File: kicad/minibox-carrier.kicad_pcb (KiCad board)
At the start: 2 copper layers, 120 x 112 mm, 14 parts, among them J1 ESP32-S3 LEFT - USB AT TOP, J11 THREE-KEY CABLE KeyA KeyB Key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, J12 JOYSTICK CABLE G V X Y K, J2 ESP32-S3 RIGHT - USB AT TOP, J3 INMP441 2x3 VDD GND / SCK WS 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, J4 MAX98357A LRC BCLK DIN GAIN S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, J5 PCF8563T CLK INT SDA SCL VCC 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, J6 ST7796 14-PIN DISPLAY HEADER, J7 5.08mm wire terminal, J8 5.08mm wire terminal

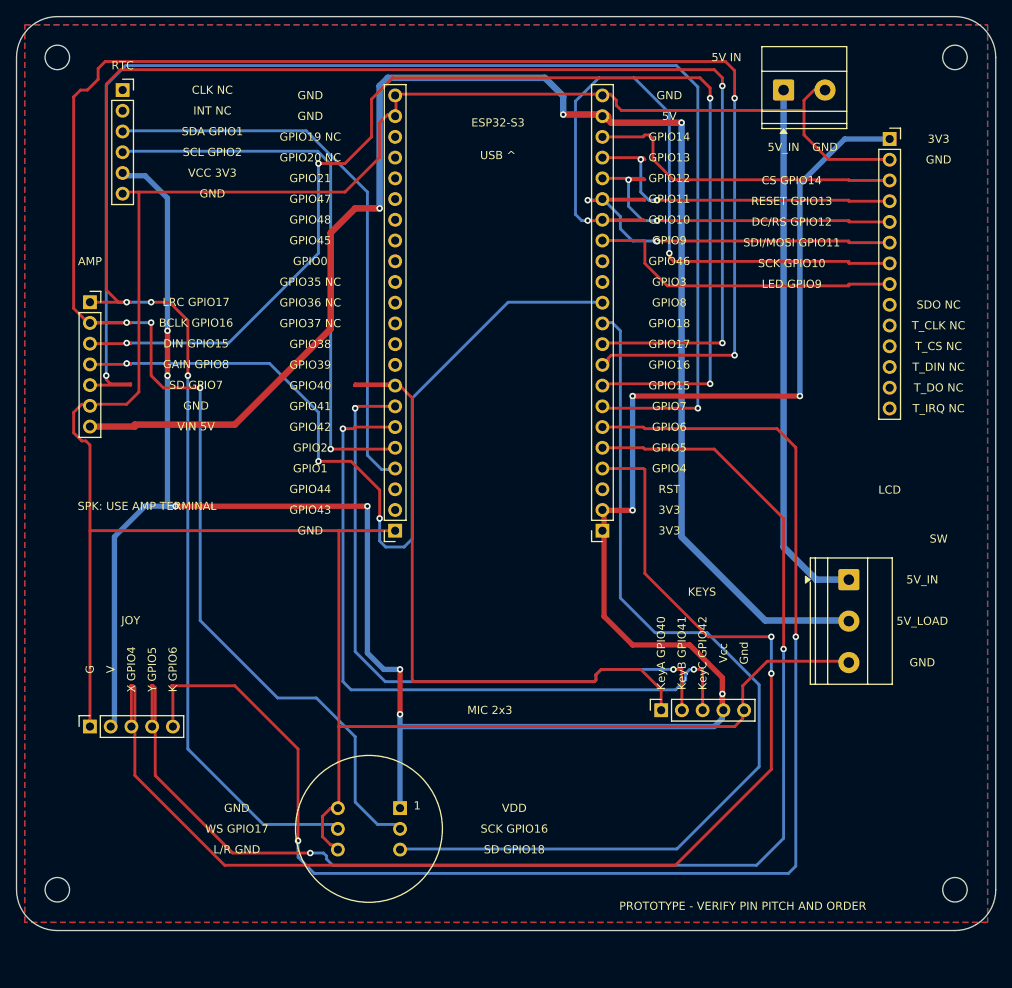
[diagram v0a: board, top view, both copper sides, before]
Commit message: Allocate GPIOs by carrier layout and move cable interfaces upward
Keep joystick axes on ADC1 GPIO1/2, keypad on GPIO4/5/6, local I2S on GPIO39/40/41 and RTC on GPIO47/21. Synchronize firmware, labels, two-layer Gerbers and PNG legends.

Co-authored-by: Copilot App <223556219+Copilot@users.noreply.github.com>
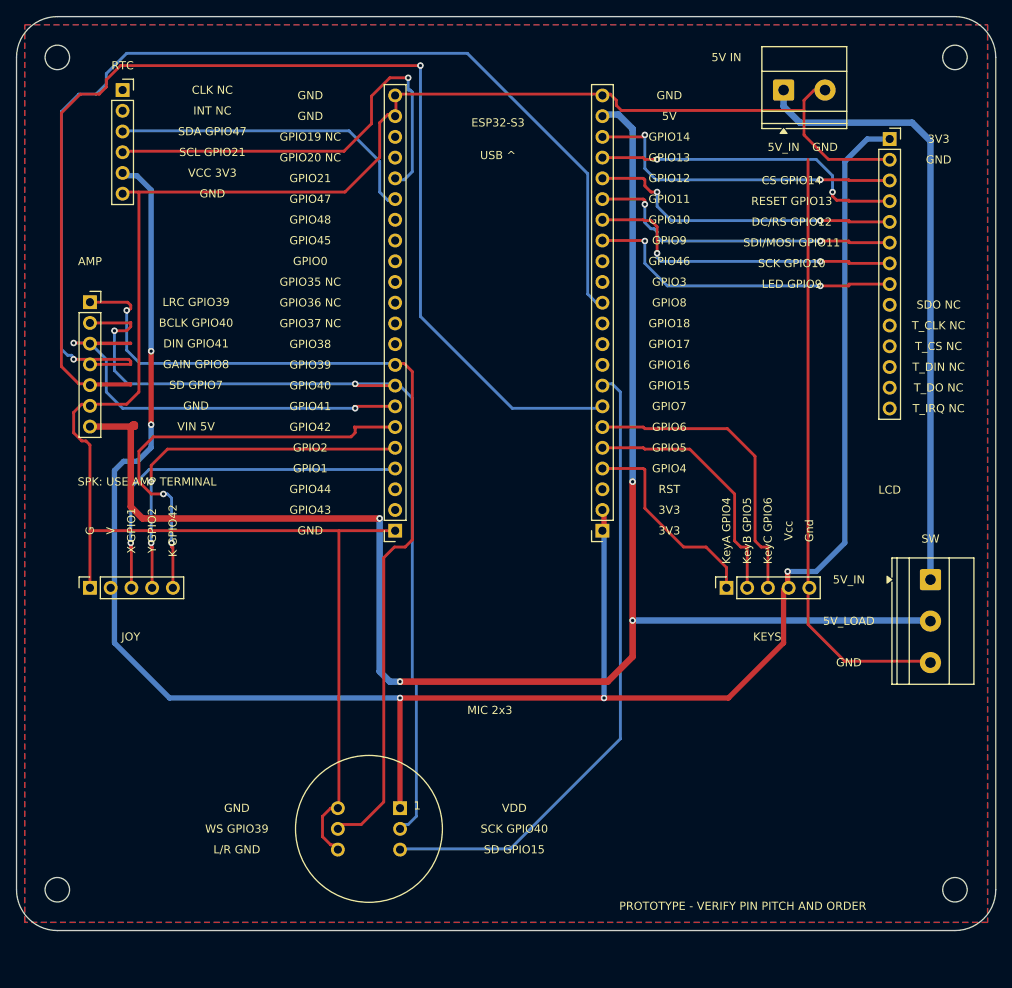
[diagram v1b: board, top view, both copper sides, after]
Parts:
- moved J11 17.0 mm to (90.0, 73.0)
- moved J12 17.0 mm to (12.0, 73.0)
- moved J7 10.0 mm to (115.0, 72.0)
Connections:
- J1 pad 10: I2S_WS -> GPIO17
- J1 pad 11: MIC_SD -> GPIO18
- J1 pad 4: GPIO4 -> BUTTON1
- J1 pad 5: GPIO5 -> RECORD
- J1 pad 6: GPIO6 -> BUTTON3
- J1 pad 8: AUDIO_DIN -> MIC_SD
- J1 pad 9: I2S_BCLK -> GPIO16
- J12 pad 3: GPIO4 -> GPIO1
- J12 pad 4: GPIO5 -> GPIO2
- J12 pad 5: GPIO6 -> GPIO42
- J2 pad 17: GPIO47 -> RTC_SDA
- J2 pad 18: GPIO21 -> RTC_SCL
- J2 pad 4: RTC_SDA -> GPIO1
- J2 pad 5: RTC_SCL -> GPIO2
- J2 pad 6: BUTTON3 -> GPIO42
- J2 pad 7: RECORD -> AUDIO_DIN
- J2 pad 8: BUTTON1 -> I2S_BCLK
- J2 pad 9: GPIO39 -> I2S_WS
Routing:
- net GPIO6: track 175.3 -> 0.00 mm, vias 2 -> 0
- net GPIO5: track 164.6 -> 0.00 mm, vias 2 -> 0
- net GPIO4: track 156.8 -> 0.00 mm, vias 2 -> 0
- net I2S_BCLK: track 259.0 -> 110.4 mm, vias 5 -> 2
- net I2S_WS: track 241.5 -> 109.6 mm, vias 5 -> 1
- net AUDIO_DIN: track 149.8 -> 57.5 mm, vias 4 -> 2
- net BUTTON1: track 82.7 -> 25.5 mm
- net GPIO42: track 0.00 -> 52.9 mm, vias 0 -> 2
- net RECORD: track 82.6 -> 31.1 mm, vias 2 -> 0
- net BUTTON3: track 88.7 -> 37.4 mm, vias 2 -> 0
- net LCD_SCK: track 87.5 -> 39.7 mm
- net GPIO2: track 0.00 -> 46.1 mm, vias 0 -> 2
- net GPIO1: track 0.00 -> 45.9 mm, vias 0 -> 1
- net MIC_SD: track 115.1 -> 77.9 mm
- net 3V3: track 296.5 -> 259.4 mm, vias 10 -> 5
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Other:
- board text added: "BCLK GPIO40"
- board text added: "DIN GPIO41"
- board text added: "K GPIO42"
- board text added: "KeyA GPIO4"
- board text added: "KeyB GPIO5"
- board text added: "KeyC GPIO6"
- board text added: "LRC GPIO39"
- board text added: "SCK GPIO40"
- board text added: "SCL GPIO21"
- board text added: "SD GPIO15"
- board text added: "SDA GPIO47"
- board text added: "WS GPIO39"
- board text added: "X GPIO1"
- board text added: "Y GPIO2"
- board text removed: "BCLK GPIO16"
- board text removed: "DIN GPIO15"
- board text removed: "K GPIO6"
- board text removed: "KeyA GPIO40"
- board text removed: "KeyB GPIO41"
- board text removed: "KeyC GPIO42"
- board text removed: "LRC GPIO17"
- board text removed: "SCK GPIO16"
- board text removed: "SCL GPIO2"
- board text removed: "SD GPIO18"
- board text removed: "SDA GPIO1"
- board text removed: "WS GPIO17"
- board text removed: "X GPIO4"
- board text removed: "Y GPIO5"

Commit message: Align switch body and eliminate right-angle trace elbows
Preserve vias and branch connectivity while easing short fanout and anchored corners. Confirm switched amplifier supply and atomically refresh matched PNG previews and two-layer Gerbers.

Co-authored-by: Copilot App <223556219+Copilot@users.noreply.github.com>
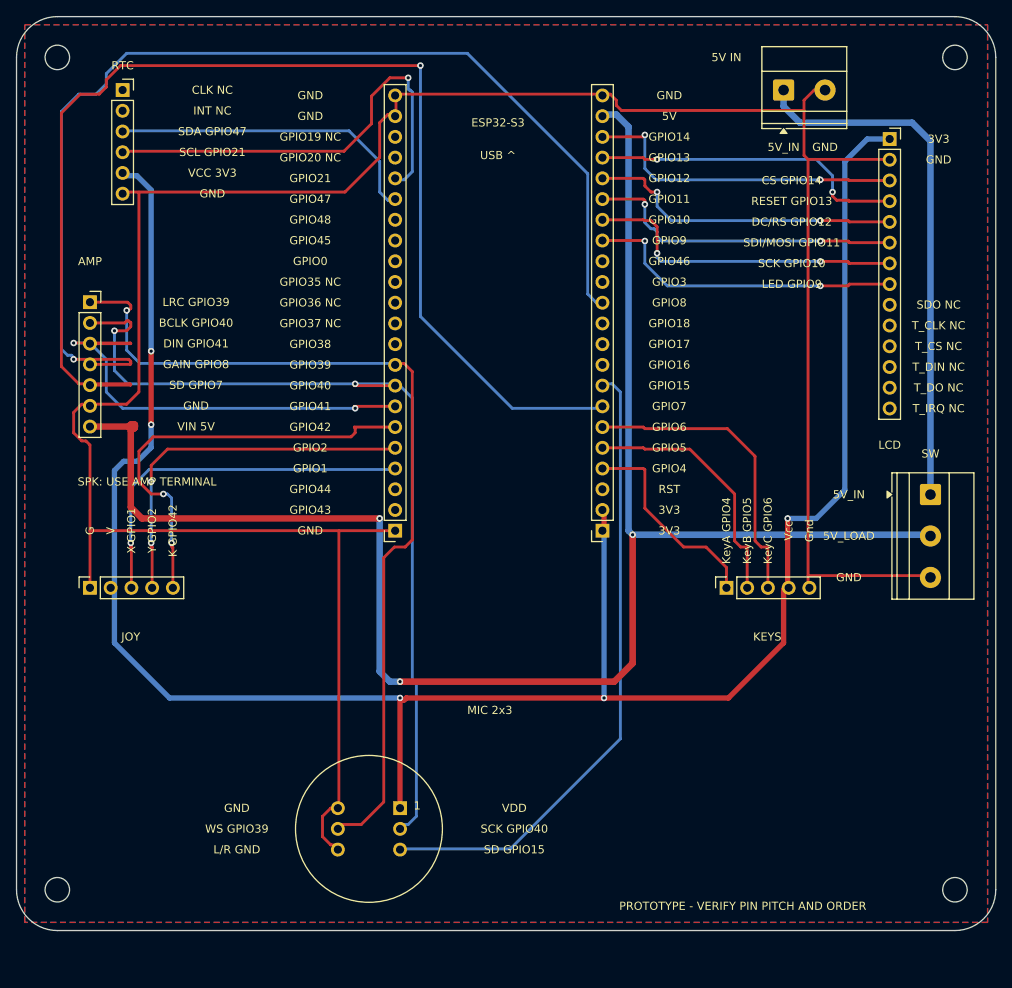
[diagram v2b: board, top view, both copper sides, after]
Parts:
- moved J7 10.4 mm to (115.0, 61.6)
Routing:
- net 5V_IN: track 75.5 -> 65.1 mm
- net GND: track 324.0 -> 318.9 mm
- net 5V_SW: track 204.6 -> 205.1 mm, vias 4 -> 3

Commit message: Compact MiniBox carrier and add manufacturing identification
Stack LCD, switch and keypad on a 100x112 mm two-layer board. Add microphone socket models, mechanical dimensions, socket inventory and v1.0 silkscreen. Enlarge safe diagonal routing and refresh fabrication and render outputs.

Co-authored-by: Copilot App <223556219+Copilot@users.noreply.github.com>
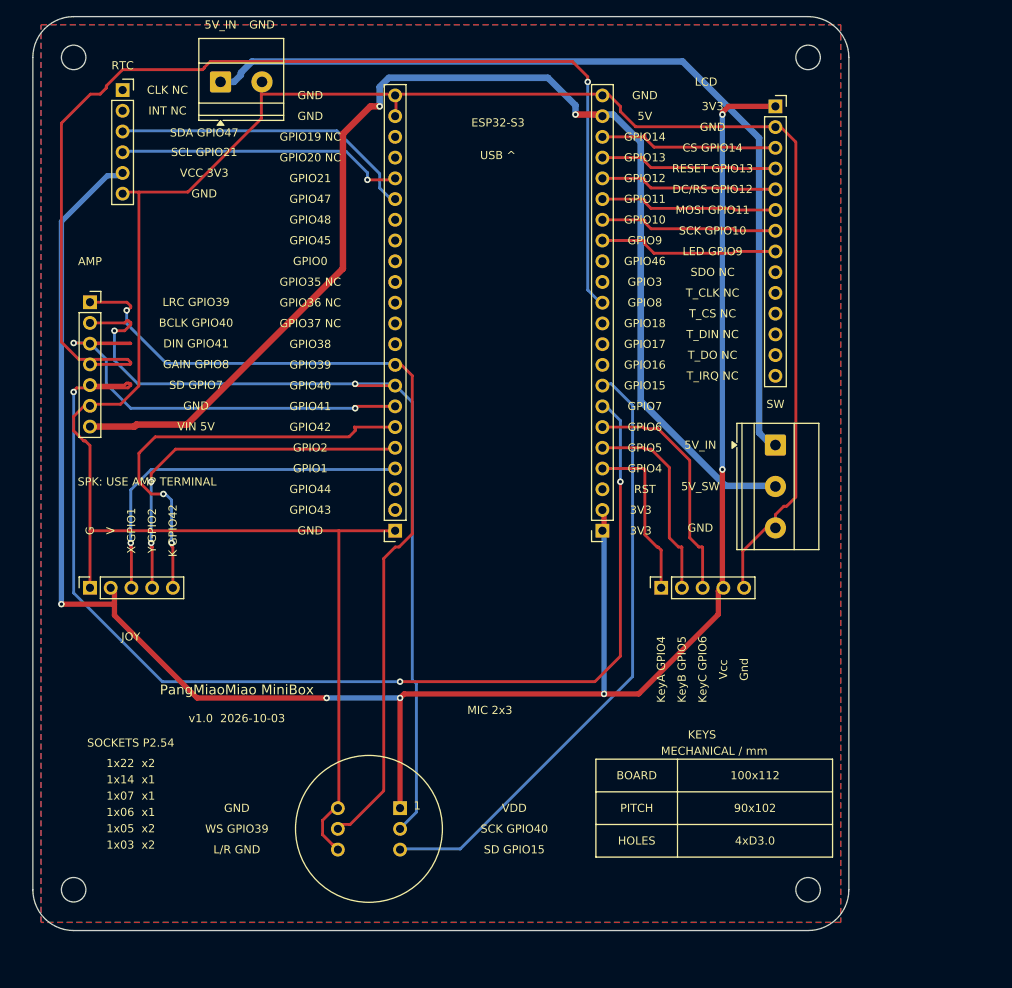
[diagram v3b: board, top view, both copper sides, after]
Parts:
- moved J8 69.0 mm to (28.0, 11.0)
- moved J7 19.9 mm to (96.0, 55.5)
- moved H2 18.0 mm to (100.0, 8.00)
- moved H4 18.0 mm to (100.0, 110.0)
- moved J6 14.6 mm to (96.0, 14.0)
- moved J11 8.00 mm to (82.0, 73.0)
- moved H1 2.00 mm to (10.0, 8.00)
- moved H3 2.00 mm to (10.0, 110.0)
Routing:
- net 5V_SW: track 205.1 -> 153.3 mm, vias 3 -> 2
- net 5V_IN: track 65.1 -> 109.8 mm
- net GND: track 318.9 -> 290.0 mm
- net RTC_SCL: track 55.2 -> 35.7 mm
- net LCD_CS: track 40.1 -> 22.2 mm, vias 2 -> 0
- net LCD_SCK: track 39.6 -> 21.9 mm, vias 2 -> 0
- net LCD_MOSI: track 39.4 -> 21.9 mm, vias 2 -> 0
- net LCD_BL: track 39.2 -> 22.1 mm, vias 2 -> 0
- net LCD_DC: track 38.9 -> 21.9 mm, vias 2 -> 0
- net LCD_RST: track 38.9 -> 21.9 mm, vias 2 -> 0
- net BUTTON3: track 37.4 -> 28.9 mm
- net AMP_SD: track 150.7 -> 142.2 mm, vias 1 -> 3
- net RECORD: track 31.1 -> 24.8 mm
- net BUTTON1: track 25.5 -> 20.6 mm
- net 3V3: track 259.5 -> 254.9 mm, vias 5 -> 6
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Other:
- board size 120 x 112 mm -> 100 x 112 mm
- board text added: "100x112"
- board text added: "1x03 x2"
- board text added: "1x05 x2"
- board text added: "1x06 x1"
- board text added: "1x07 x1"
- board text added: "1x14 x1"
- board text added: "1x22 x2"
- board text added: "4xD3.0"
- board text added: "5V_SW"
- board text added: "90x102"
- board text added: "BOARD"
- board text added: "HOLES"
- board text added: "MECHANICAL / mm"
- board text added: "MOSI GPIO11"
- board text added: "PITCH"
- board text added: "PangMiaoMiao MiniBox"
- board text added: "SOCKETS P2.54"
- board text added: "v1.0 2026-10-03"
- board text removed: "5V IN"
- board text removed: "5V_LOAD"
- board text removed: "PROTOTYPE - VERIFY PIN PITCH AND ORDER"
- board text removed: "SDI/MOSI GPIO11"

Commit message: Convert MiniBox carrier to four layers with continuous I2S ground reference
Co-authored-by: Copilot App <223556219+Copilot@users.noreply.github.com>
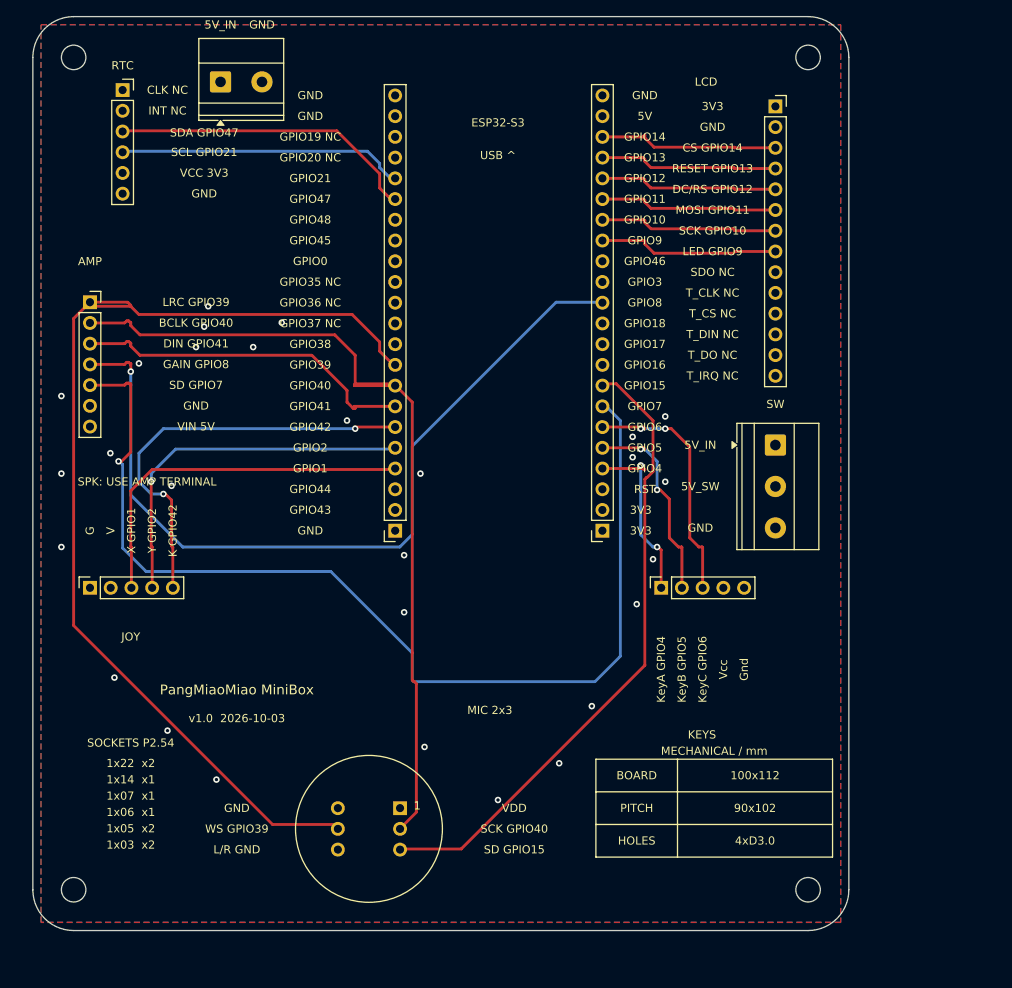
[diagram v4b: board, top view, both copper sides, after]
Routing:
- net GND: track 290.0 -> 0.00 mm, vias 0 -> 28
- net AMP_GAIN: track 139.1 -> 101.1 mm
- net I2S_WS: track 105.9 -> 129.8 mm, vias 1 -> 0
- net AUDIO_DIN: track 56.9 -> 42.4 mm, vias 2 -> 0
- net 3V3: track 254.9 -> 242.1 mm, vias 6 -> 0
- net AMP_SD: track 142.2 -> 129.4 mm, vias 3 -> 1
- net 5V_IN: track 109.8 -> 103.2 mm
- net 5V_SW: track 153.3 -> 148.9 mm, vias 2 -> 0
- net I2S_BCLK: track 109.0 -> 105.0 mm, vias 2 -> 0
- net MIC_SD: track 75.4 -> 78.0 mm
- net BUTTON3: track 28.9 -> 30.9 mm, vias 0 -> 2
- net BUTTON1: track 20.6 -> 22.4 mm, vias 0 -> 2
- net RECORD: track 24.8 -> 25.6 mm, vias 0 -> 2
- net RTC_SCL: track 35.7 -> 35.5 mm, vias 1 -> 0
- net GPIO1: vias 1 -> 0
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- added copper zone on In2.Cu, net 3V3
- added copper zone on In2.Cu, net 5V_IN
- added copper zone on In2.Cu, net 5V_SW
- added copper zone on In1.Cu, net GND
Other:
- copper layers 2 -> 4
